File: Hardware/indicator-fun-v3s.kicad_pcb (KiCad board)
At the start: 2 copper layers, 100 x 100 mm, 166 parts, among them IC1 LM1117, IC2 MD8002A, J1 TRANSFLASH-LOCK, J2 AUDIO_JACK_SMD, J3 USB_B_Micro OTG, J4 Power, Q2 32kHz, Q3 BSS138, SW1 Reset, SW2 BOOT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

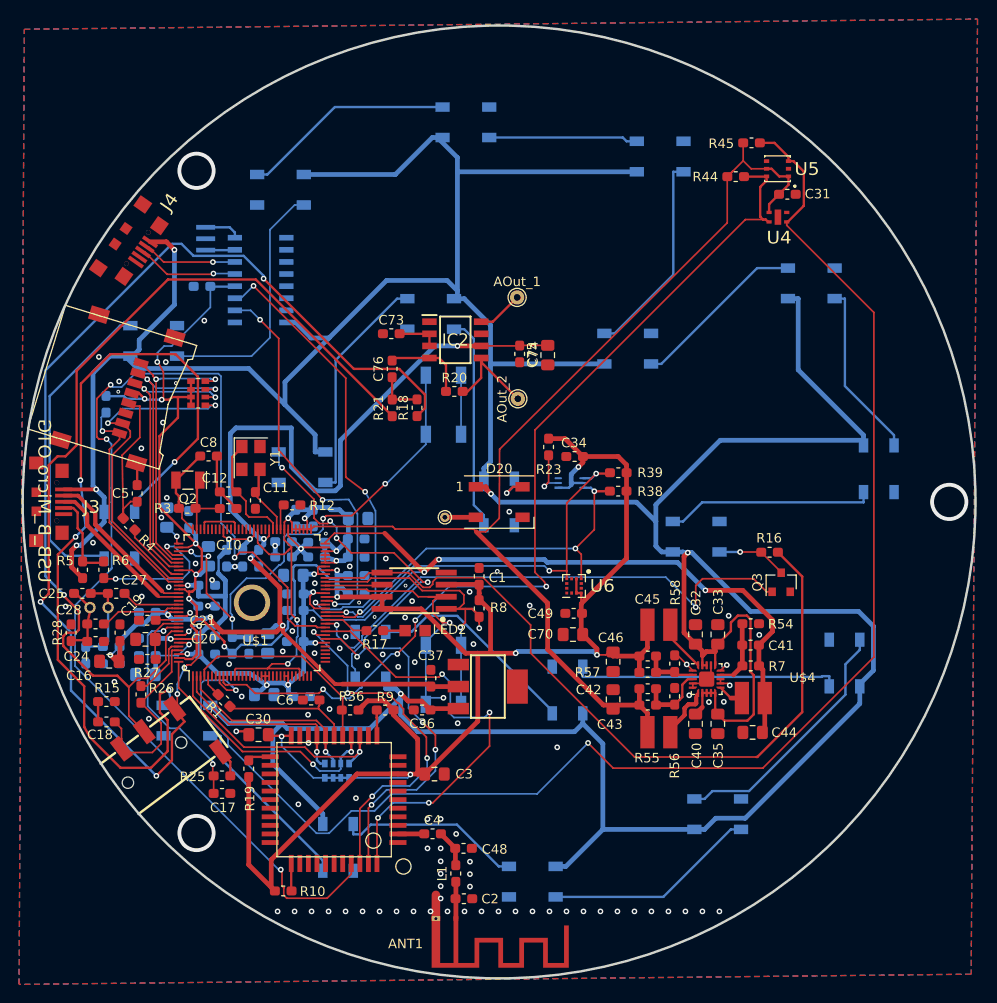
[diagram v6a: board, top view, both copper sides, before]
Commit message: Разведена шина AGND
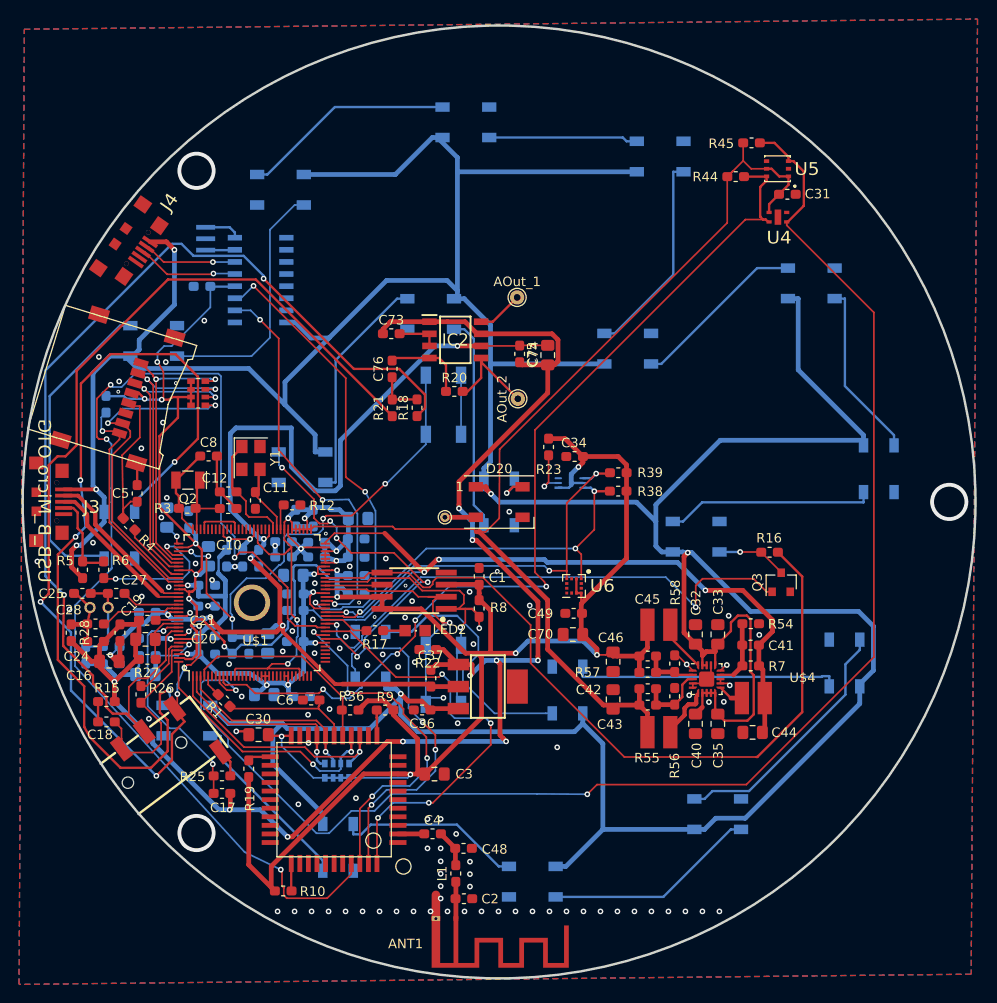
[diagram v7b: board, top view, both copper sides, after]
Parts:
- added R22: 0, Resistor_SMD:R_0603_1608Metric_Pad1.05x0.95mm_HandSolder, F.Cu at (139.9, 111.0)
- C20: value 10µF -> 4.7µF
- turned R28 to 270 degrees
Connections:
- C16 pad 1: GND -> AGND
- C17 pad 2: GND -> AGND
- C19 pad 1: GND -> AGND
- C20 pad 1: GND -> AGND
- C21 pad 1: GND -> AGND
- C22 pad 2: GND -> AGND
- C23 pad 1: GND -> AGND
- C24 pad 1: GND -> AGND
- C26 pad 1: GND -> AGND
- C29 pad 1: GND -> AGND
- C37 pad 2: GND -> AGND
- C73 pad 1: GND -> AGND
- C74 pad 2: GND -> AGND
- C75 pad 1: GND -> AGND
- IC1 pad 1: GND -> AGND
- IC2 pad 1: GND -> AGND
- IC2 pad 7: GND -> AGND
- R15 pad 1: GND -> AGND
- R27 pad 1: GND -> AGND
- R28 pad 2: GND -> AGND
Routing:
- net AGND: track 0.00 -> 179.0 mm, vias 0 -> 10
- net Net-(D15-Pad2): track 22.6 -> 27.7 mm
- net SDA-1.8: track 158.5 -> 156.3 mm
- net /WLAN/UART2/RTS/PB2: track 46.6 -> 45.7 mm
- net +3V3: track 293.7 -> 294.6 mm
- net LED_CTL: track 80.9 -> 81.5 mm
- net /USB-SDC0-Audio/HP_R: track 109.4 -> 110.0 mm
- net /WLAN/SPI1/CS: track 33.0 -> 33.6 mm
- net /Power/x32kin: track 10.3 -> 9.80 mm

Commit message: Добавлен вырез под динамик
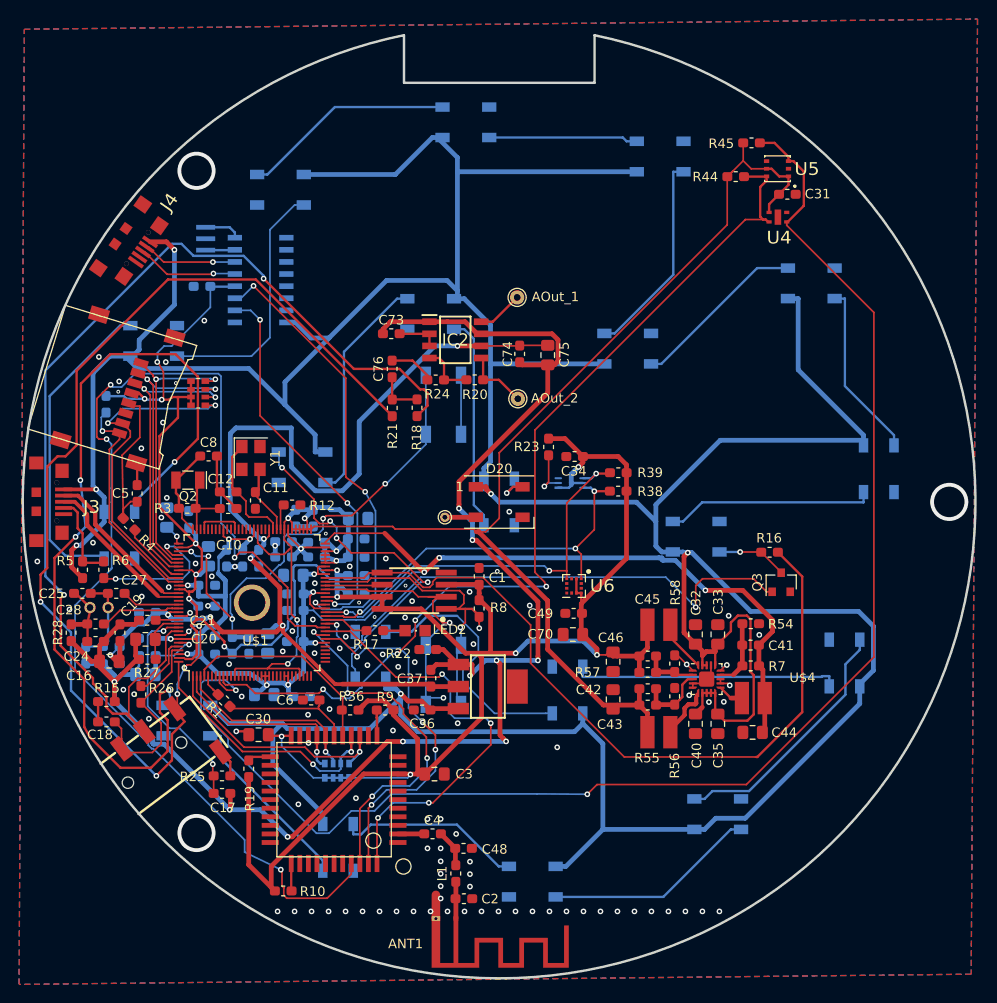
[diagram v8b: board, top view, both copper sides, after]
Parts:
- added R24: 22k, Resistor_SMD:R_0603_1608Metric_Pad1.05x0.95mm_HandSolder, F.Cu at (140.7, 82.7)
- C76: value 100nF -> 0.22µF
- J3: value USB_B_Micro OTG -> USB OTG
- J4: value Power -> Power\Console
- R20: value 22k -> 68k
- moved R20 2.47 mm to (144.8, 82.7)
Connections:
- IC2 pad 4: Net-(C76-Pad2) -> Net-(IC2-Pad4)
- R20 pad 1: Net-(C76-Pad2) -> Net-(IC2-Pad4)
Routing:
- net Net-(IC2-Pad4): track 0.00 -> 5.88 mm
- net Net-(C76-Pad2): track 8.85 -> 5.20 mm
- net Net-(AOut_2-Pad1): track 10.5 -> 6.84 mm
- net AGND: track 179.0 -> 177.3 mm
- net UART0/RX: track 41.5 -> 40.2 mm
- net /USB-SDC0-Audio/HP_R: track 110.0 -> 110.7 mm
- net /WLAN/UART2/CTS/PB3: track 122.6 -> 123.2 mm
- net GND: vias 106 -> 109
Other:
- board size 100 x 100 mm -> 100 x 99 mm
- board text added: "Ver. 1.2 www.indicator.fun"
- board text removed: "Ver. 1.1 www.indicator.fun"
